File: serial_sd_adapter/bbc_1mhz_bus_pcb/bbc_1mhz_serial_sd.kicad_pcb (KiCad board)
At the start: 2 copper layers, 48.3 x 53.3 mm, 20 parts, among them U1 MCP1700T-3302E/MB, U2 Pro Micro 5V

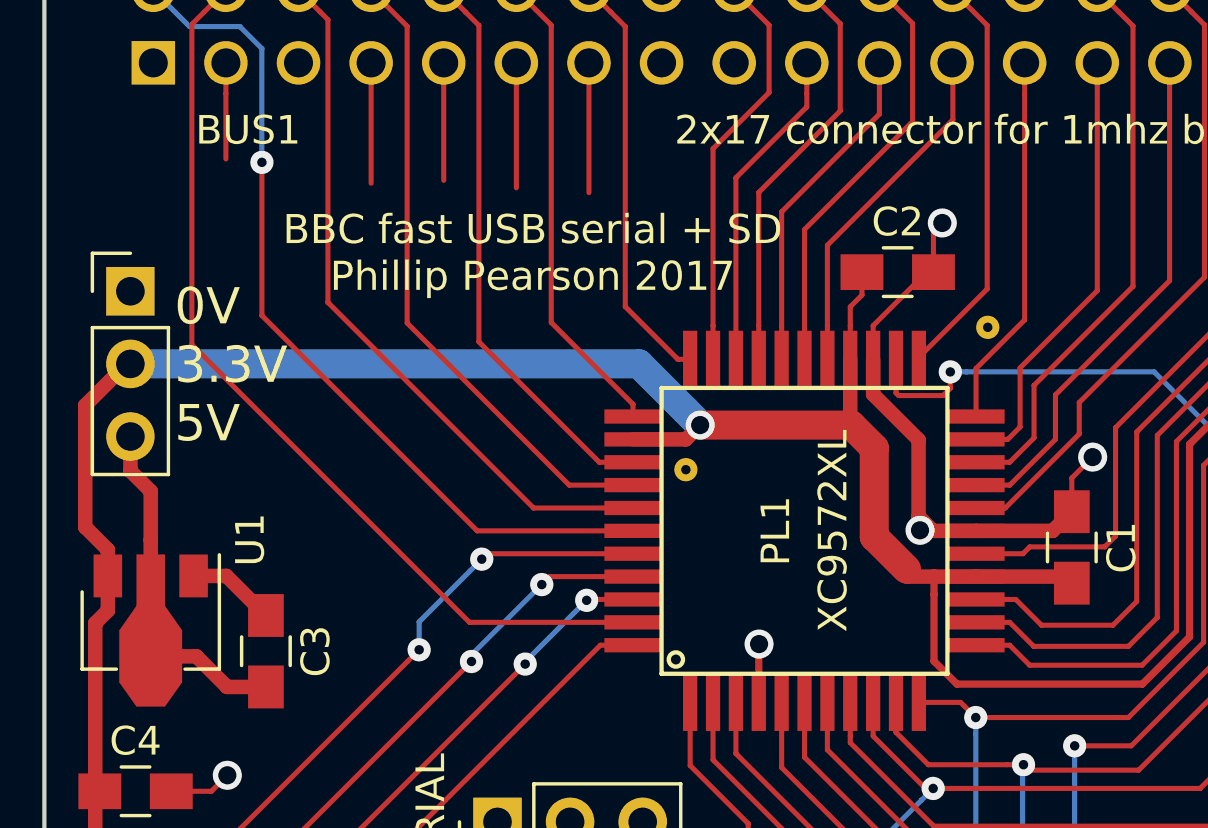
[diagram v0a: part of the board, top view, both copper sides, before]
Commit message: Renamed some signals to match VHDL, and updated TODOs for r2
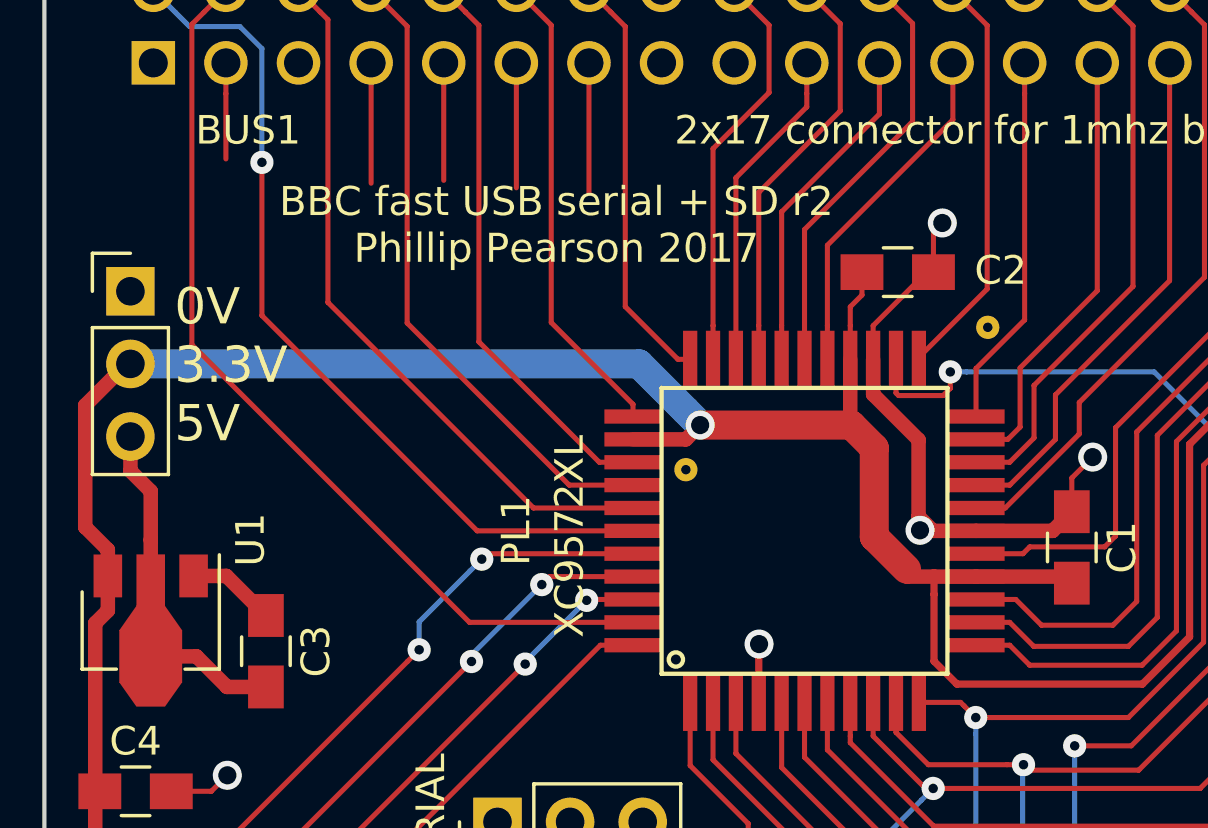
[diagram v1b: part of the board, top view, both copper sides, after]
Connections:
- net avr_SD_SEL renamed avr_nSD_SEL
- net avr_SS renamed avr_nSS
- net sd_SS renamed sd_nSS
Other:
- board text added: "BBC fast USB serial + SD for the 1 MHz Bus serial_sd_adapter/bbc_1mhz_bus_pcb r2 Copyright 2017 Google Inc"
- board text added: "BBC fast USB serial + SD r2 Phillip Pearson 2017"
- board text removed: "BBC fast USB serial + SD Phillip Pearson 2017"
- board text removed: "BBC fast USB serial + SD for the 1 MHz Bus Copyright 2017 Google Inc"
